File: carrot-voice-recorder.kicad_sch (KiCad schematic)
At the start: 0 parts

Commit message: added initial speaker circuit
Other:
- added sheet Speaker Driver Circuit (SpeakerDriver.kicad_sch)
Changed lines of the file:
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@@
 	(generator_version "9.0")
 	(paper "A4")
+	(sheet
+		(at 114.3 74.93)
+		(size 34.29 20.32)
+		(exclude_from_sim no)
+		(in_bom yes)
+		(on_board yes)
+		(dnp no)
+		(fields_autoplaced yes)
+		(stroke
+			(width 0.1524)
+			(type solid)
+		)
+		(fill
+			(color 0 0 0 0.0000)
+		)
+		(property "Sheetname" "Speaker Driver Circuit"
+			(at 114.3 74.2184 0)
+			(effects
+				(font
+					(size 1.27 1.27)
+				)
+				(justify left bottom)
+			)
+		)
+		(property "Sheetfile" "SpeakerDriver.kicad_sch"
+			(at 114.3 95.8346 0)
+			(effects
+				(font
+					(size 1.27 1.27)
+				)
+				(justify left top)
+			)
+		)
+		(pin "SPEAKER_I2S_LRCLK" input
+			(at 114.3 85.09 180)
+			(effects
+				(font
+					(size 1.27 1.27)
+				)
+				(justify left)
+			)
+		)
+		(pin "SPEAKER_I2S_MCLK" input
+			(at 114.3 88.9 180)
+			(effects
+				(font
+					(size 1.27 1.27)
+				)
+				(justify left)
+			)
+		)
+		(pin "SPEAKER_I2S_SLCK" input
+			(at 114.3 81.28 180)
+			(effects
+				(font
+					(size 1.27 1.27)
+				)
+				(justify left)
+			)
+		)
+		(pin "SPEAKER_I2S_SDA" input
+			(at 114.3 77.47 180)
+			(effects
+				(font
+					(size 1.27 1.27)
+				)
+				(justify left)
+			)
+		)
+		(pin "SPEAKER_SIGNAL" output
+			(at 148.59 92.71 0)
+			(effects
+				(font
+					(size 1.27 1.27)
+				)
+				(justify right)
+			)
+		)
+		(instances
+			(project "carrot-voice-recorder"
+				(path "/6e73c62c-3b38-4fda-9d84-b2b702c58c74"
+					(page "2")
+				)
+			)
+		)
+	)
 	(sheet_instances
 		(path "/"

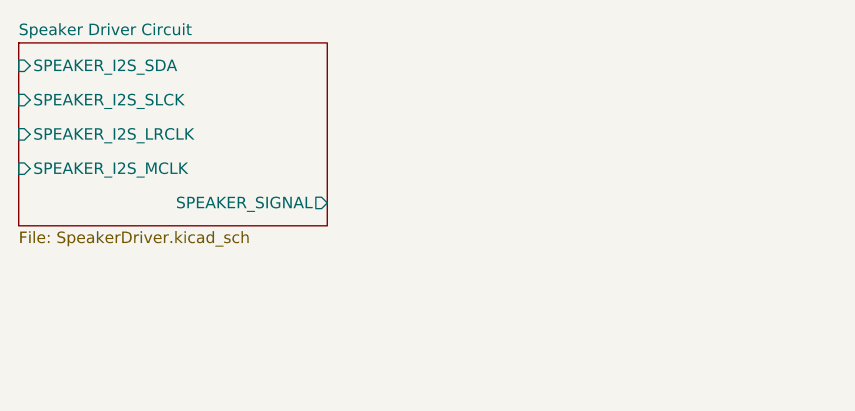
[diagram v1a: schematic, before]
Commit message: create esp32 sch
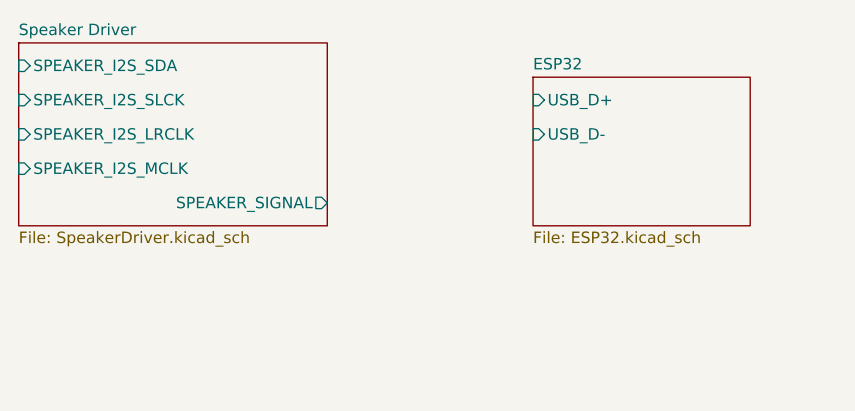
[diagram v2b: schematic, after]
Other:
- sheet Speaker Driver Circuit renamed Speaker Driver
- added sheet ESP32 (ESP32.kicad_sch)
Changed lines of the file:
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@@
 	(paper "A4")
+	(sheet
+		(at 171.45 78.74)
+		(size 24.13 16.51)
+		(exclude_from_sim no)
+		(in_bom yes)
+		(on_board yes)
+		(dnp no)
+		(fields_autoplaced yes)
+		(stroke
+			(width 0.1524)
+			(type solid)
+		)
+		(fill
+			(color 0 0 0 0.0000)
+		)
+		(property "Sheetname" "ESP32"
+			(at 171.45 78.0284 0)
+			(effects
+				(font
+					(size 1.27 1.27)
+				)
+				(justify left bottom)
+			)
+		)
+		(property "Sheetfile" "ESP32.kicad_sch"
+			(at 171.45 95.8346 0)
+			(effects
+				(font
+					(size 1.27 1.27)
+				)
+				(justify left top)
+			)
+		)
+		(pin "USB_D+" input
+			(at 171.45 81.28 180)
+			(effects
+				(font
+					(size 1.27 1.27)
+				)
+				(justify left)
+			)
+		)
+		(pin "USB_D-" input
+			(at 171.45 85.09 180)
+			(effects
+				(font
+					(size 1.27 1.27)
+				)
+				(justify left)
+			)
+		)
+		(instances
+			(project "carrot-voice-recorder"
+				(path "/6e73c62c-3b38-4fda-9d84-b2b702c58c74"
+					(page "3")
+				)
+			)
+		)
+	)
 	(sheet
 		(at 114.3 74.93)
@@
 			(color 0 0 0 0.0000)
 		)
-		(property "Sheetname" "Speaker Driver Circuit"
+		(property "Sheetname" "Speaker Driver"
 			(at 114.3 74.2184 0)
 			(effects

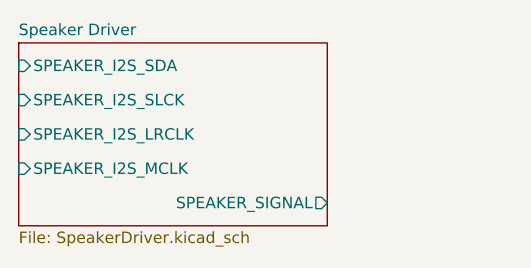
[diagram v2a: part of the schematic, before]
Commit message: fix sclk typo
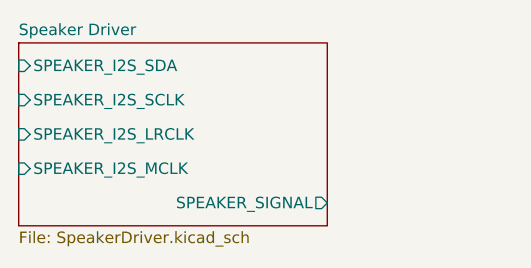
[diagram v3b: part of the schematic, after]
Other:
- sheet Speaker Driver ports: added SPEAKER_I2S_SCLK; removed SPEAKER_I2S_SLCK
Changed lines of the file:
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@@
 			)
 		)
-		(pin "SPEAKER_I2S_SLCK" input
+		(pin "SPEAKER_I2S_SCLK" input
 			(at 114.3 81.28 180)
 			(effects

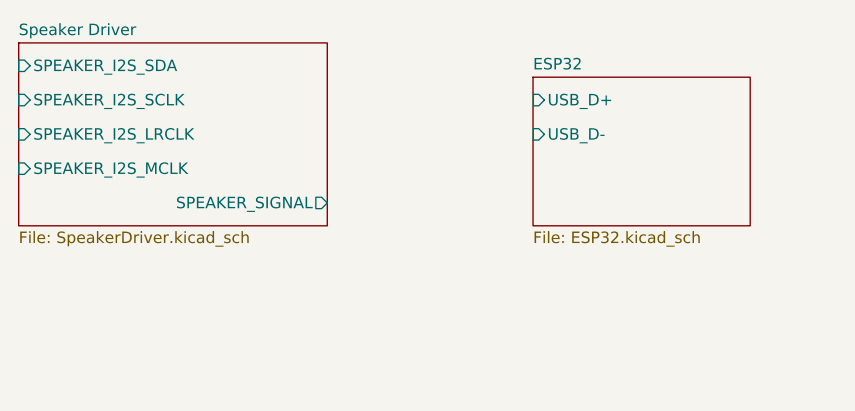
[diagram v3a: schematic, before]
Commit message: finish esp32 hierarchical flags
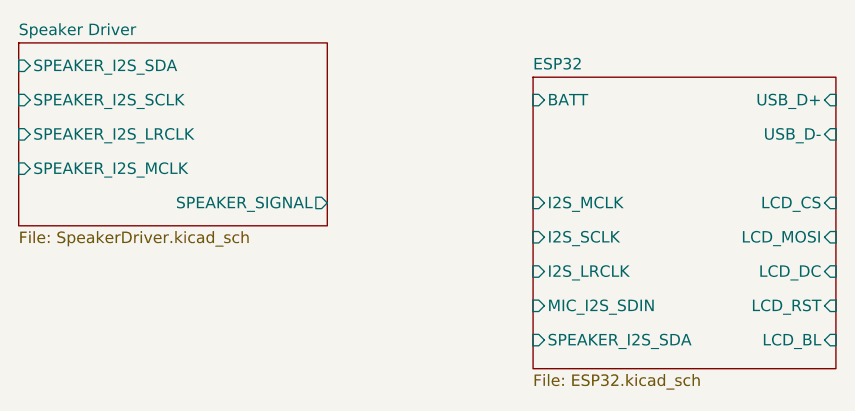
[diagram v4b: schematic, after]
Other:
- sheet ESP32 ports: added BATT, I2S_LRCLK, I2S_MCLK, I2S_SCLK, LCD_BL, LCD_CS, LCD_DC, LCD_MOSI, LCD_RST, MIC_I2S_SDIN, SPEAKER_I2S_SDA; removed none
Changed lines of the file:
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@@
 	(sheet
 		(at 171.45 78.74)
-		(size 24.13 16.51)
+		(size 33.655 32.385)
 		(exclude_from_sim no)
 		(in_bom yes)
@@
 		)
 		(property "Sheetfile" "ESP32.kicad_sch"
-			(at 171.45 95.8346 0)
+			(at 171.45 111.7096 0)
 			(effects
 				(font
@@
 		)
 		(pin "USB_D+" input
+			(at 205.105 81.28 0)
+			(effects
+				(font
+					(size 1.27 1.27)
+				)
+				(justify right)
+			)
+		)
+		(pin "USB_D-" input
+			(at 205.105 85.09 0)
+			(effects
+				(font
+					(size 1.27 1.27)
+				)
+				(justify right)
+			)
+		)
+		(pin "LCD_BL" input
+			(at 205.105 107.95 0)
+			(effects
+				(font
+					(size 1.27 1.27)
+				)
+				(justify right)
+			)
+		)
+		(pin "MIC_I2S_SDIN" input
+			(at 171.45 104.14 180)
+			(effects
+				(font
+					(size 1.27 1.27)
+				)
+				(justify left)
+			)
+		)
+		(pin "LCD_CS" input
+			(at 205.105 92.71 0)
+			(effects
+				(font
+					(size 1.27 1.27)
+				)
+				(justify right)
+			)
+		)
+		(pin "I2S_SCLK" input
+			(at 171.45 96.52 180)
+			(effects
+				(font
+					(size 1.27 1.27)
+				)
+				(justify left)
+			)
+		)
+		(pin "I2S_LRCLK" input
+			(at 171.45 100.33 180)
+			(effects
+				(font
+					(size 1.27 1.27)
+				)
+				(justify left)
+			)
+		)
+		(pin "BATT" input
 			(at 171.45 81.28 180)
 			(effects
@@
 			)
 		)
-		(pin "USB_D-" input
-			(at 171.45 85.09 180)
+		(pin "I2S_MCLK" input
+			(at 171.45 92.71 180)
 			(effects
 				(font
+					(size 1.27 1.27)
+				)
+				(justify left)
+			)
+		)
+		(pin "LCD_MOSI" input
+			(at 205.105 96.52 0)
+			(effects
+				(font
+					(size 1.27 1.27)
+				)
+				(justify right)
+			)
+		)
+		(pin "LCD_RST" input
+			(at 205.105 104.14 0)
+			(effects
+				(font
+					(size 1.27 1.27)
+				)
+				(justify right)
+			)
+		)
+		(pin "LCD_DC" input
+			(at 205.105 100.33 0)
+			(effects
+				(font
+					(size 1.27 1.27)
+				)
+				(justify right)
+			)
+		)
+		(pin "SPEAKER_I2S_SDA" input
+			(at 171.45 107.95 180)
+			(effects
+				(font
